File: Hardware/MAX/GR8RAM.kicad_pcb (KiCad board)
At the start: 4 copper layers, 99.9 x 59.8 mm, 87 parts, among them J1 AppleIIBus, J2 JTAG, J3 microUSB, J5 Flash, SW1 FW, U1 EPM240T100C5N, U10 AP2127K-1.8TRG1, U11 74LVC1G125GW, U13 25M, U14 74LVC1G125GW, U16 74LVC1G125GW, U2 W9825, U3 W25Q128JVSIQ, U4 74AHC245PW, U5 74AHC245PW, U6 74AHC245PW, U7 CH340G, U8 XC6206P332MR, U9 74AHC245PW, Y1 12M

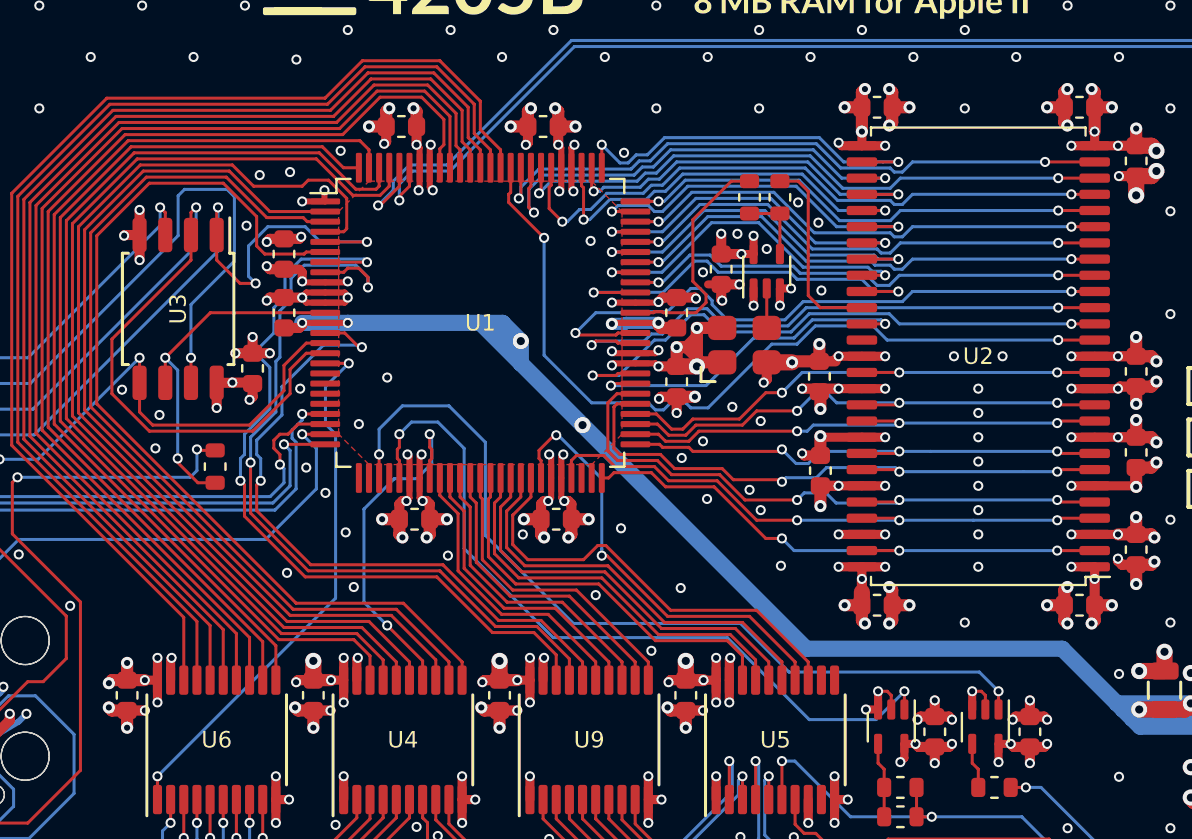
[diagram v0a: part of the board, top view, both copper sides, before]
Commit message: Adopt 0.5mm via-to-via spacing
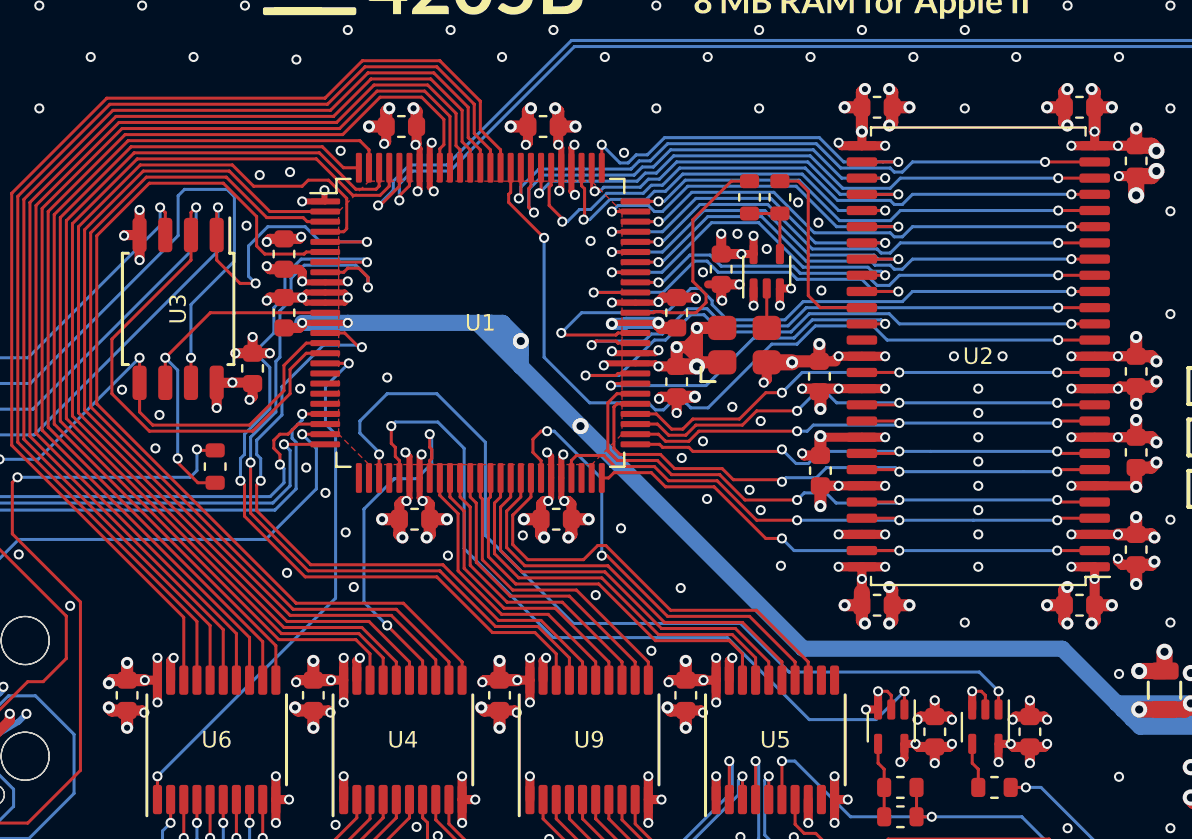
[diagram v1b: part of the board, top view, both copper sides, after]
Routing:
- net +1V8: track 115.4 -> 117.8 mm
- net /IRQ~{OE}: track 42.9 -> 45.0 mm
- net /S~{RAS}: track 30.9 -> 32.3 mm
- net /R~{RES}: track 22.1 -> 23.0 mm
- net +3V3: track 165.8 -> 166.5 mm
- net /RES~{OE}: track 37.9 -> 38.6 mm
- net /S~{WE}: track 29.1 -> 29.8 mm
- net GND: track 221.6 -> 221.1 mm, vias 475 -> 473
